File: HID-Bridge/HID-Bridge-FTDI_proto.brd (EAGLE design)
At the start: 34.3 x 22.9 mm, 7 parts, among them U1 FT232RLSSOP

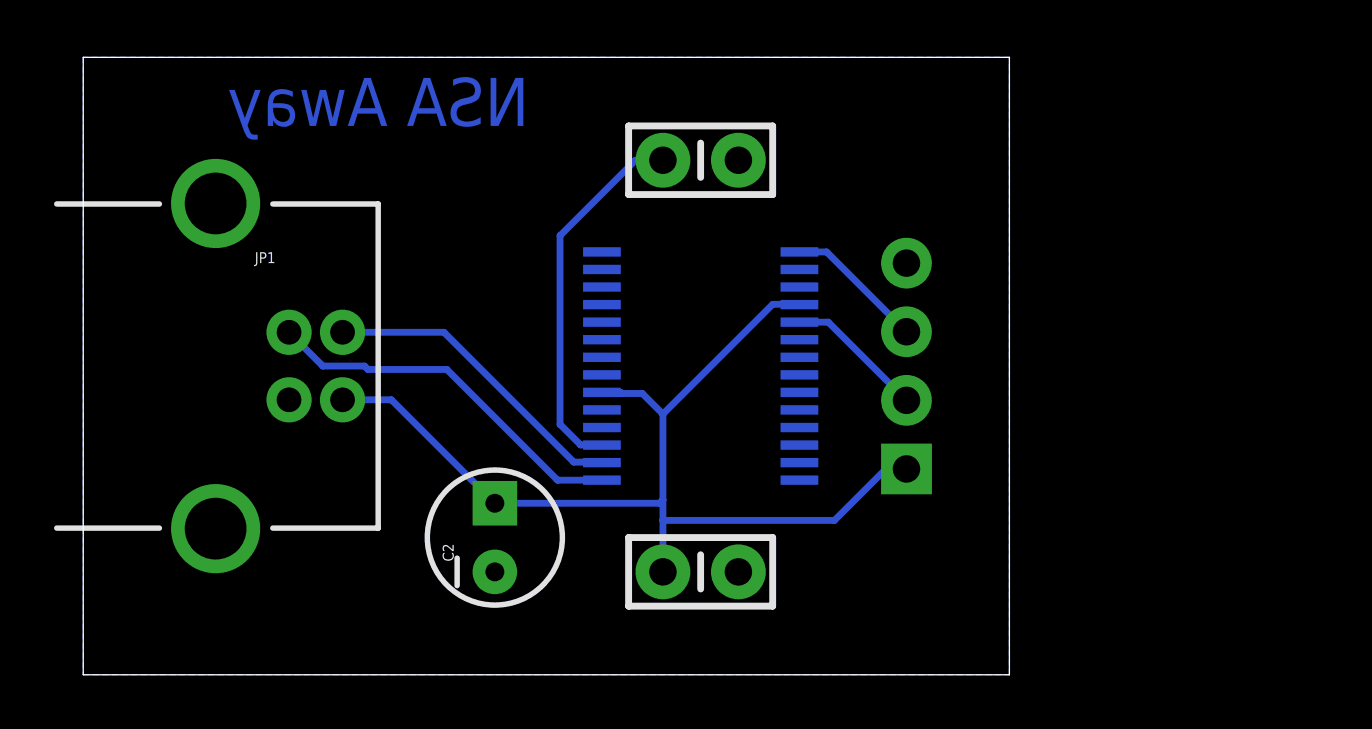
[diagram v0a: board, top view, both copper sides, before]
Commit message: Changes on FTDI, larger clearance &c
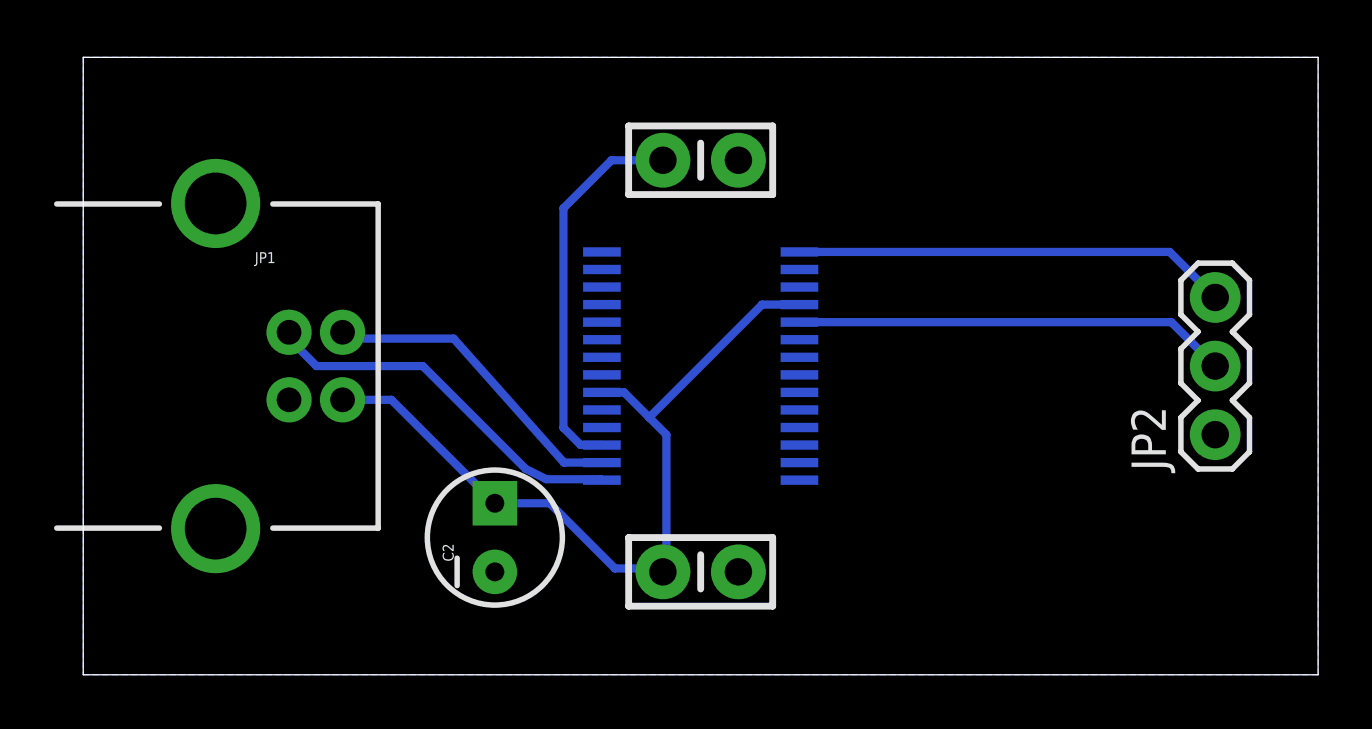
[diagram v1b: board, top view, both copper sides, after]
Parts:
- JP2: device SparkFun-Connectors:1X04 -> SparkFun-Connectors:1X03
- moved JP2 11.5 mm to (41.9, 8.89), flipped to the top
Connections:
- net 5V: no longer JP2.1
- net GND: now also JP2.1; no longer JP2.4
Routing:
- net N$4: track 5.19 -> 16.1 mm
- net N$1: track 5.16 -> 16.1 mm
- net 5V: track 38.5 -> 30.0 mm
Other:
- board size 34.3 x 22.9 mm -> 45.7 x 22.9 mm
- board text removed: "NSA Away"
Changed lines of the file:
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@@
 <board>
 <plain>
-<wire x1="0" y1="0" x2="34.29" y2="0" width="0" layer="20"/>
-<wire x1="34.29" y1="0" x2="34.29" y2="22.86" width="0" layer="20"/>
-<wire x1="34.29" y1="22.86" x2="0" y2="22.86" width="0" layer="20"/>
+<wire x1="0" y1="0" x2="45.72" y2="0" width="0" layer="20"/>
+<wire x1="45.72" y1="0" x2="45.72" y2="22.86" width="0" layer="20"/>
+<wire x1="45.72" y1="22.86" x2="0" y2="22.86" width="0" layer="20"/>
 <wire x1="0" y1="22.86" x2="0" y2="0" width="0" layer="20"/>
 <text x="26.67" y="26.67" size="1.778" layer="51" font="vector" ratio="15">Liam Marshall</text>
-<text x="16.51" y="20.32" size="1.778" layer="16" font="vector" ratio="15" rot="MR0">NSA Away</text>
 </plain>
 <attributes>
@@
 <attribute name="PROD_ID" value="CAP-08370" x="39.37" y="-13.97" size="1.778" layer="27" display="off"/>
 </element>
-<element name="JP2" library="SparkFun-Connectors" package="1X04" value="" x="30.48" y="7.62" rot="MR90"/>
+<element name="JP2" library="SparkFun-Connectors" package="1X03" value="" x="41.91" y="8.89" rot="R90"/>
 </elements>
 <signals>
@@
 <contactref element="U1" pad="18"/>
 <contactref element="U1" pad="21"/>
-<contactref element="JP2" pad="4"/>
-<polygon width="0.254" layer="16" isolate="0.254">
+<polygon width="0.254" layer="16" isolate="0.2794">
 <vertex x="0" y="22.86"/>
 <vertex x="0" y="0"/>
-<vertex x="34.29" y="0"/>
-<vertex x="34.29" y="22.86"/>
+<vertex x="45.72" y="0"/>
+<vertex x="45.72" y="22.86"/>
 </polygon>
+<contactref element="JP2" pad="1"/>
 <wire x1="19.204" y1="9.155" x2="19.204" y2="11.105" width="0" layer="19" extent="16-16"/>
-<wire x1="26.516" y1="11.755" x2="30.48" y2="15.24" width="0" layer="19" extent="16-16"/>
 </signal>
 <signal name="N$2">
 <contactref element="JP1" pad="D+"/>
 <contactref element="U1" pad="15"/>
-<wire x1="19.204" y1="7.205" x2="17.56" y2="7.205" width="0.254" layer="16"/>
-<wire x1="17.56" y1="7.205" x2="13.462" y2="11.303" width="0.254" layer="16"/>
-<wire x1="13.462" y1="11.303" x2="10.541" y2="11.303" width="0.254" layer="16"/>
-<wire x1="10.541" y1="11.303" x2="10.414" y2="11.43" width="0.254" layer="16"/>
-<wire x1="10.414" y1="11.43" x2="8.87" y2="11.43" width="0.254" layer="16"/>
-<wire x1="8.87" y1="11.43" x2="7.62" y2="12.68" width="0.254" layer="16"/>
+<wire x1="7.62" y1="12.68" x2="7.62" y2="12.446" width="0.3048" layer="16"/>
+<wire x1="7.62" y1="12.446" x2="8.636" y2="11.43" width="0.3048" layer="16"/>
+<wire x1="8.636" y1="11.43" x2="12.573" y2="11.43" width="0.3048" layer="16"/>
+<wire x1="12.573" y1="11.43" x2="16.383" y2="7.62" width="0.3048" layer="16"/>
+<wire x1="16.383" y1="7.62" x2="17.145" y2="7.239" width="0.3048" layer="16"/>
+<wire x1="17.145" y1="7.239" x2="19.17" y2="7.239" width="0.3048" layer="16"/>
+<wire x1="19.17" y1="7.239" x2="19.204" y2="7.205" width="0.3048" layer="16"/>
 </signal>
 <signal name="N$3">
 <contactref element="JP1" pad="D-"/>
 <contactref element="U1" pad="16"/>
-<wire x1="9.6012" y1="12.68" x2="13.355" y2="12.68" width="0.254" layer="16"/>
-<wire x1="13.355" y1="12.68" x2="18.161" y2="7.874" width="0.254" layer="16"/>
-<wire x1="18.161" y1="7.874" x2="19.185" y2="7.874" width="0.254" layer="16"/>
-<wire x1="19.185" y1="7.874" x2="19.204" y2="7.855" width="0.254" layer="16"/>
+<wire x1="19.204" y1="7.855" x2="17.799" y2="7.855" width="0.3048" layer="16"/>
+<wire x1="17.799" y1="7.855" x2="13.716" y2="12.446" width="0.3048" layer="16"/>
+<wire x1="13.716" y1="12.446" x2="9.8352" y2="12.446" width="0.3048" layer="16"/>
+<wire x1="9.8352" y1="12.446" x2="9.6012" y2="12.68" width="0.3048" layer="16"/>
 </signal>
 <signal name="5V">
@@
 <contactref element="U1" pad="20"/>
 <contactref element="U1" pad="4"/>
-<contactref element="JP2" pad="1"/>
-<wire x1="9.6012" y1="10.18" x2="11.41" y2="10.18" width="0.254" layer="16"/>
-<wire x1="11.41" y1="10.18" x2="15.24" y2="6.35" width="0.254" layer="16"/>
-<wire x1="21.463" y1="3.81" x2="21.463" y2="5.715" width="0.254" layer="16"/>
-<wire x1="21.463" y1="5.715" x2="21.463" y2="6.477" width="0.254" layer="16"/>
-<wire x1="21.463" y1="6.477" x2="21.463" y2="9.652" width="0.254" layer="16"/>
-<wire x1="21.463" y1="9.652" x2="25.527" y2="13.716" width="0.254" layer="16"/>
-<wire x1="25.527" y1="13.716" x2="26.505" y2="13.716" width="0.254" layer="16"/>
-<wire x1="26.505" y1="13.716" x2="26.516" y2="13.705" width="0.254" layer="16"/>
-<wire x1="15.24" y1="6.35" x2="21.336" y2="6.35" width="0.254" layer="16"/>
-<wire x1="21.336" y1="6.35" x2="21.463" y2="6.477" width="0.254" layer="16"/>
-<wire x1="30.48" y1="7.62" x2="29.718" y2="7.62" width="0.254" layer="16"/>
-<wire x1="29.718" y1="7.62" x2="27.813" y2="5.715" width="0.254" layer="16"/>
-<wire x1="27.813" y1="5.715" x2="21.463" y2="5.715" width="0.254" layer="16"/>
-<wire x1="19.204" y1="10.455" x2="19.898" y2="10.455" width="0.254" layer="16"/>
-<wire x1="19.898" y1="10.455" x2="19.939" y2="10.414" width="0.254" layer="16"/>
-<wire x1="19.939" y1="10.414" x2="20.701" y2="10.414" width="0.254" layer="16"/>
-<wire x1="20.701" y1="10.414" x2="21.463" y2="9.652" width="0.254" layer="16"/>
+<wire x1="9.6012" y1="10.18" x2="11.41" y2="10.18" width="0.3048" layer="16"/>
+<wire x1="11.41" y1="10.18" x2="15.24" y2="6.35" width="0.3048" layer="16"/>
+<wire x1="15.24" y1="6.35" x2="17.272" y2="6.35" width="0.3048" layer="16"/>
+<wire x1="17.272" y1="6.35" x2="19.685" y2="3.937" width="0.3048" layer="16"/>
+<wire x1="19.685" y1="3.937" x2="21.336" y2="3.937" width="0.3048" layer="16"/>
+<wire x1="21.336" y1="3.937" x2="21.463" y2="3.81" width="0.3048" layer="16"/>
+<wire x1="19.204" y1="10.455" x2="20.025" y2="10.455" width="0.3048" layer="16"/>
+<wire x1="20.025" y1="10.455" x2="20.955" y2="9.525" width="0.3048" layer="16"/>
+<wire x1="20.955" y1="9.525" x2="21.59" y2="8.89" width="0.3048" layer="16"/>
+<wire x1="21.59" y1="8.89" x2="21.59" y2="3.937" width="0.3048" layer="16"/>
+<wire x1="21.59" y1="3.937" x2="21.463" y2="3.81" width="0.3048" layer="16"/>
+<wire x1="26.516" y1="13.705" x2="25.135" y2="13.705" width="0.3048" layer="16"/>
+<wire x1="25.135" y1="13.705" x2="20.955" y2="9.525" width="0.3048" layer="16"/>
 </signal>
 <signal name="3.3V">
 <contactref element="U1" pad="17"/>
 <contactref element="C3" pad="1"/>
-<wire x1="21.463" y1="19.05" x2="20.447" y2="19.05" width="0.254" layer="16"/>
-<wire x1="20.447" y1="19.05" x2="17.653" y2="16.256" width="0.254" layer="16"/>
-<wire x1="17.653" y1="16.256" x2="17.653" y2="9.271" width="0.254" layer="16"/>
-<wire x1="17.653" y1="9.271" x2="18.415" y2="8.509" width="0.254" layer="16"/>
-<wire x1="18.415" y1="8.509" x2="19.2" y2="8.509" width="0.254" layer="16"/>
-<wire x1="19.2" y1="8.509" x2="19.204" y2="8.505" width="0.254" layer="16"/>
+<wire x1="21.463" y1="19.05" x2="19.558" y2="19.05" width="0.3048" layer="16"/>
+<wire x1="19.558" y1="19.05" x2="17.78" y2="17.272" width="0.3048" layer="16"/>
+<wire x1="17.78" y1="17.272" x2="17.78" y2="9.144" width="0.3048" layer="16"/>
+<wire x1="17.78" y1="9.144" x2="18.415" y2="8.509" width="0.3048" layer="16"/>
+<wire x1="18.415" y1="8.509" x2="19.2" y2="8.509" width="0.3048" layer="16"/>
+<wire x1="19.2" y1="8.509" x2="19.204" y2="8.505" width="0.3048" layer="16"/>
 </signal>
 <signal name="N$1">
 <contactref element="JP2" pad="2"/>
 <contactref element="U1" pad="5"/>
-<wire x1="26.516" y1="13.055" x2="27.585" y2="13.055" width="0.254" layer="16"/>
-<wire x1="27.585" y1="13.055" x2="30.48" y2="10.16" width="0.254" layer="16"/>
+<wire x1="26.516" y1="13.055" x2="40.285" y2="13.055" width="0.3048" layer="16"/>
+<wire x1="40.285" y1="13.055" x2="41.91" y2="11.43" width="0.3048" layer="16"/>
 </signal>
 <signal name="N$4">
 <contactref element="U1" pad="1"/>
 <contactref element="JP2" pad="3"/>
-<wire x1="26.516" y1="15.655" x2="27.525" y2="15.655" width="0.254" layer="16"/>
-<wire x1="27.525" y1="15.655" x2="30.48" y2="12.7" width="0.254" layer="16"/>
+<wire x1="26.516" y1="15.655" x2="40.225" y2="15.655" width="0.3048" layer="16"/>
+<wire x1="40.225" y1="15.655" x2="41.91" y2="13.97" width="0.3048" layer="16"/>
 </signal>
 </signals>
